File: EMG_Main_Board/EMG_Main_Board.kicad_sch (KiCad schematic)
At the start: 4 parts, among them J1 ADC input, J2 USB_C_Receptacle, U1 STM32G0B1MET6, U2 IS1871SF-102

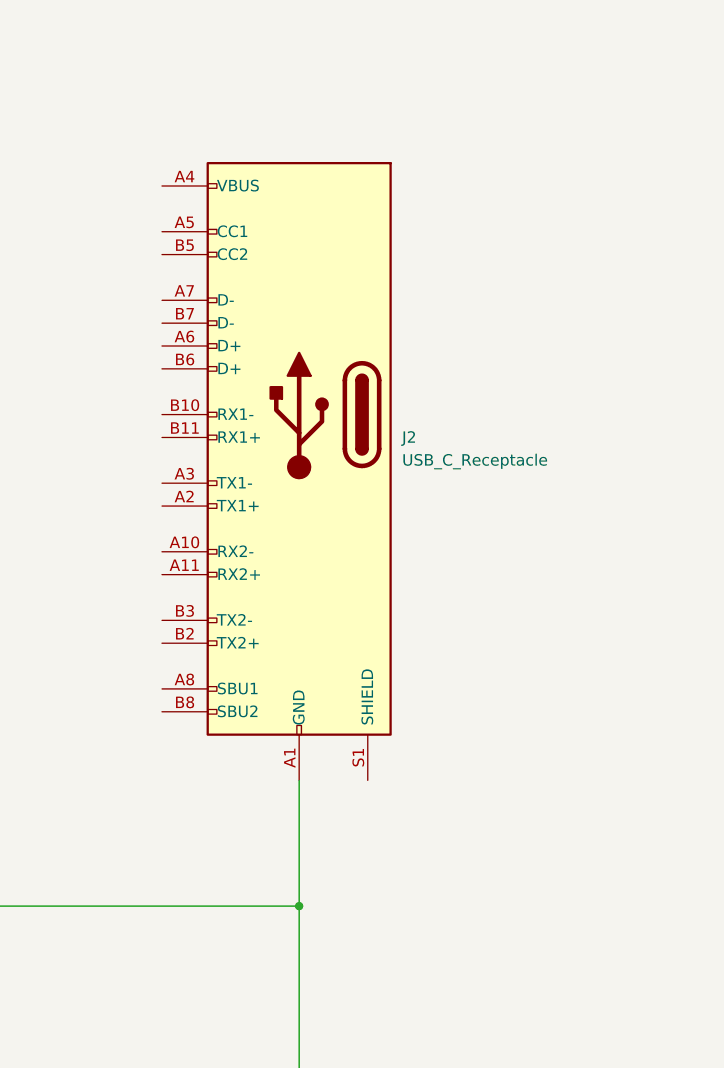
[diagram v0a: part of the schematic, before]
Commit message: add capacitor to ESD
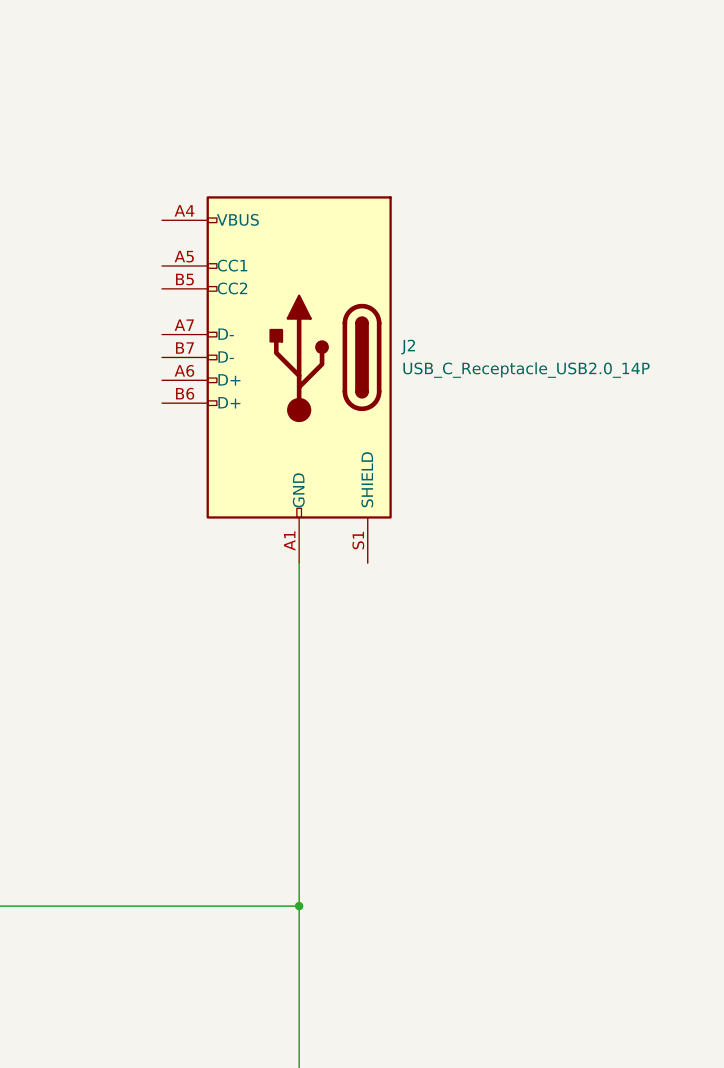
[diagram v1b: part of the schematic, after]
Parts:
- removed J2: USB_C_Receptacle, Connector_USB:USB_C_Receptacle_Amphenol_12401548E4-2A, symbol Connector:USB_C_Receptacle
- added J2: USB_C_Receptacle_USB2.0_14P, symbol Connector:USB_C_Receptacle_USB2.0_14P
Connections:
- net GND: now also J2.A1 (GND), J2.A12 (GND), J2.B1 (GND), J2.B12 (GND)
- new net: J2.A4 (VBUS), J2.A9 (VBUS), J2.B4 (VBUS), J2.B9 (VBUS)
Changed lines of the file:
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@@
 	(wire
 		(pts
-			(xy 243.84 115.57) (xy 243.84 129.54)
+			(xy 243.84 91.44) (xy 243.84 129.54)
 		)
 		(stroke
@@
 	)
 	(symbol
+		(lib_id "Connector:USB_C_Receptacle_USB2.0_14P")
+		(at 243.84 68.58 0)
+		(mirror y)
+		(unit 1)
+		(exclude_from_sim no)
+		(in_bom yes)
+		(on_board yes)
+		(dnp no)
+		(fields_autoplaced yes)
+		(property "Reference" "J2"
+			(at 255.27 67.3099 0)
+			(effects
+				(font
+					(size 1.27 1.27)
+				)
+				(justify right)
+			)
+		)
+		(property "Value" "USB_C_Receptacle_USB2.0_14P"
+			(at 255.27 69.8499 0)
+			(effects
+				(font
+					(size 1.27 1.27)
+				)
+				(justify right)
+			)
+		)
+		(property "Footprint" ""
+			(at 240.03 68.58 0)
+			(effects
+				(font
+					(size 1.27 1.27)
+				)
+				(hide yes)
+			)
+		)
+		(property "Datasheet" "https://www.usb.org/sites/default/files/documents/usb_type-c.zip"
+			(at 240.03 68.58 0)
+			(effects
+				(font
+					(size 1.27 1.27)
+				)
+				(hide yes)
+			)
+		)
+		(property "Description" "USB 2.0-only 14P Type-C Receptacle connector"
+			(at 243.84 68.58 0)
+			(effects
+				(font
+					(size 1.27 1.27)
+				)
+				(hide yes)
+			)
+		)
+		(pin "A12"
+		)
+		(pin "A4"
+		)
+		(pin "B4"
+		)
+		(pin "B6"
+		)
+		(pin "B7"
+		)
+		(pin "B5"
+		)
+		(pin "A5"
+		)
+		(pin "A1"
+		)
+		(pin "A7"
+		)
+		(pin "A9"
+		)
+		(pin "B12"
+		)
+		(pin "S1"
+		)
+		(pin "A6"
+		)
+		(pin "B1"
+		)
+		(pin "B9"
+		)
+		(instances
+			(project ""
+				(path "/f342d0b6-fa79-42c3-b491-044d5cde1fcc"
+					(reference "J2")
+					(unit 1)
+				)
+			)
+		)
+	)
+	(symbol
 		(lib_id "power:+3V3")
 		(at 113.03 24.13 0)
@@
 					(unit 1)
 				)
-			)
-		)
-	)
-	(symbol
-		(lib_id "Connector:USB_C_Receptacle")
-		(at 243.84 74.93 0)
-		(mirror y)
-		(unit 1)
-		(exclude_from_sim no)
-		(in_bom yes)
-		(on_board yes)
-		(dnp no)
-		(fields_autoplaced yes)
-		(property "Reference" "J2"
-			(at 255.27 77.4699 0)
-			(effects
-				(font
-					(size 1.27 1.27)
-				)
-				(justify right)
-			)
-		)
-		(property "Value" "USB_C_Receptacle"
-			(at 255.27 80.0099 0)
-			(effects
-				(font
-					(size 1.27 1.27)
-				)
-				(justify right)
-			)
-		)
-		(property "Footprint" "Connector_USB:USB_C_Receptacle_Amphenol_12401548E4-2A"
-			(at 240.03 74.93 0)
-			(effects
-				(font
-					(size 1.27 1.27)
-				)
-				(hide yes)
-			)
-		)
-		(property "Datasheet" "https://www.usb.org/sites/default/files/documents/usb_type-c.zip"
-			(at 240.03 74.93 0)
-			(effects
-				(font
-					(size 1.27 1.27)
-				)
-				(hide yes)
-			)
-		)
-		(property "Description" "USB Full-Featured Type-C Receptacle connector"
-			(at 243.84 74.93 0)
-			(effects
-				(font
-					(size 1.27 1.27)
-				)
-				(hide yes)
-			)
-		)
-		(pin "A1"
-		)
-		(pin "A3"
-		)
-		(pin "A6"
-		)
-		(pin "A7"
-		)
-		(pin "A9"
-		)
-		(pin "A2"
-		)
-		(pin "B12"
-		)
-		(pin "B2"
-		)
-		(pin "B3"
-		)
-		(pin "A4"
-		)
-		(pin "B4"
-		)
-		(pin "B6"
-		)
-		(pin "B11"
-		)
-		(pin "B5"
-		)
-		(pin "A5"
-		)
-		(pin "B10"
-		)
-		(pin "B1"
-		)
-		(pin "A11"
-		)
-		(pin "A8"
-		)
-		(pin "A12"
-		)
-		(pin "A10"
-		)
-		(pin "B9"
-		)
-		(pin "S1"
-		)
-		(pin "B8"
-		)
-		(pin "B7"
-		)
-		(instances
-			(project ""
-				(path "/f342d0b6-fa79-42c3-b491-044d5cde1fcc"
-					(reference "J2")
-					(unit 1)
-				)

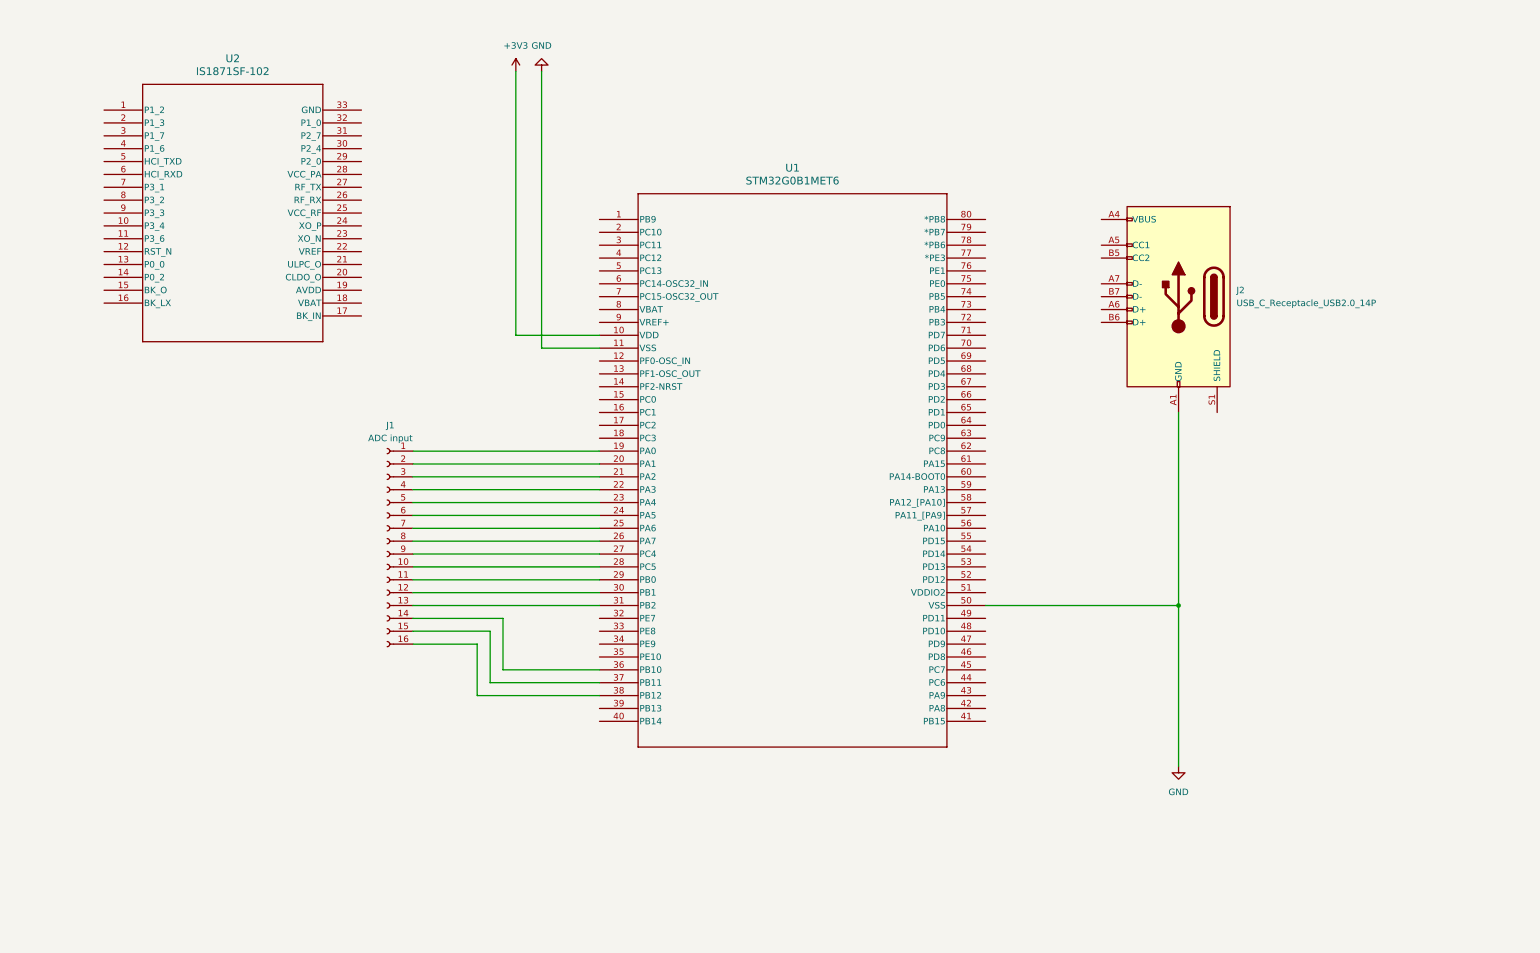
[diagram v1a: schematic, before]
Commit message: add MCU and BLE to main board schematic
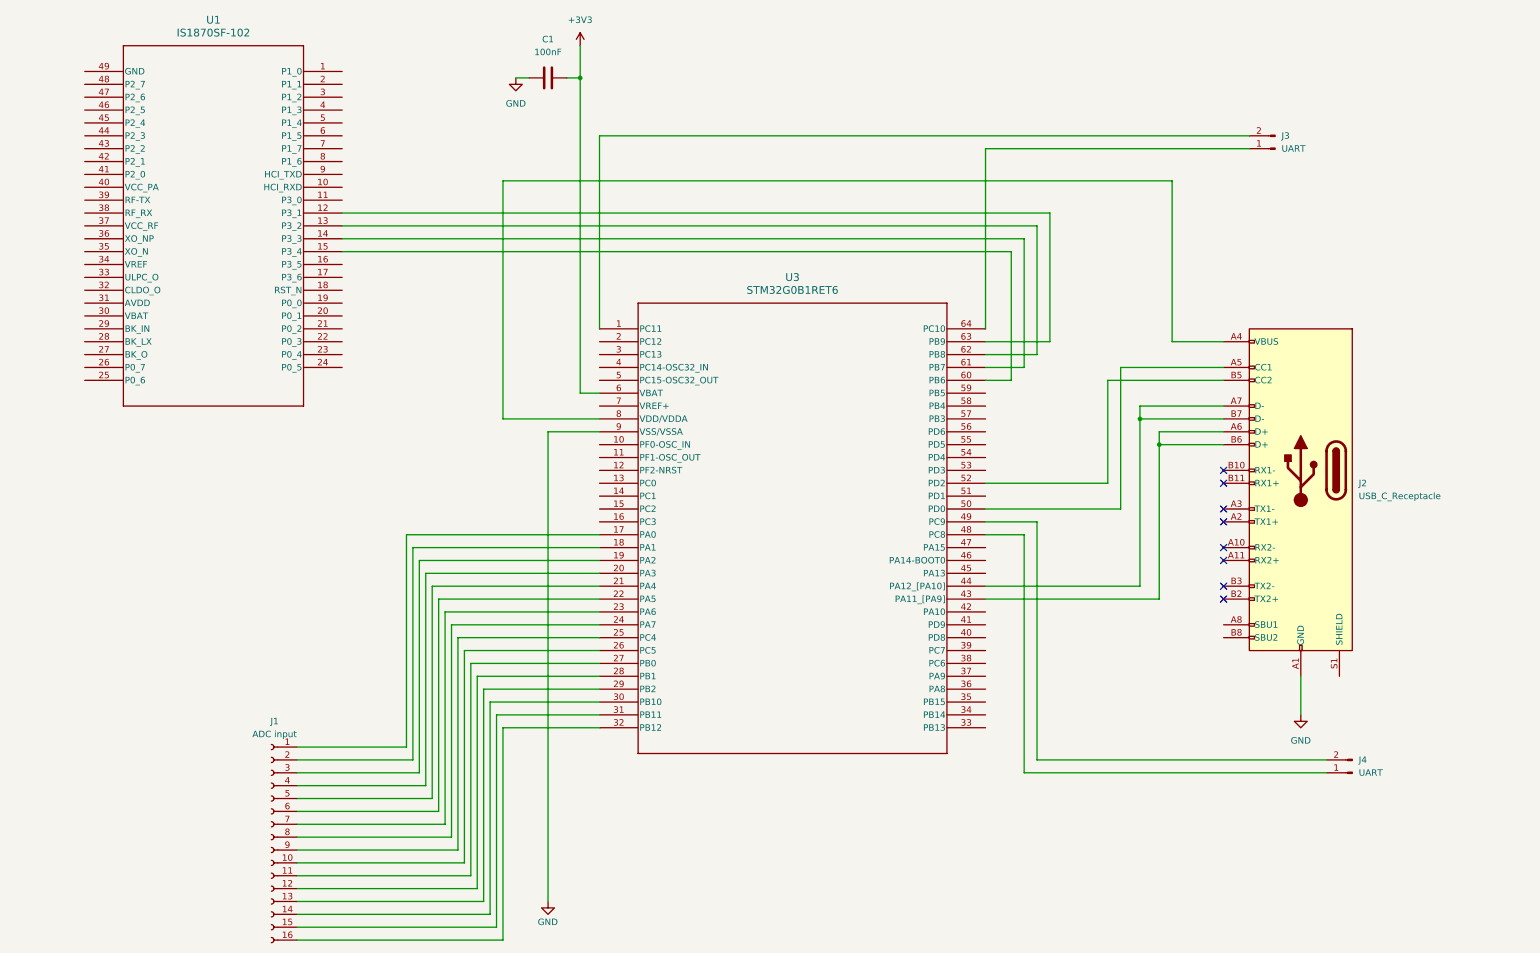
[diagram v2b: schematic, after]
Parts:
- removed J2: USB_C_Receptacle_USB2.0_14P, symbol Connector:USB_C_Receptacle_USB2.0_14P
- removed U1: STM32G0B1MET6, TQFP_0B1MET6_STM, symbol STM32G0B1MET6:STM32G0B1MET6
- removed U2: IS1871SF-102, 32QFN_4X4_IS1871SF_MCH, symbol IS1871:IS1871SF-102
- added C1: 100nF, symbol Device:C
- added J2: USB_C_Receptacle, symbol Connector:USB_C_Receptacle
- added J3, J4: UART, symbol Connector:Conn_01x02_Pin
- added U1: IS1870SF-102, 48QFN_6X6_IS1870SF_MCH, symbol IS1870SF-102:IS1870SF-102
- added U3: STM32G0B1RET6, STM32G0B1RET6:LQFP_0B1RET6_STM, symbol STM32G0B1RET6:STM32G0B1RET6
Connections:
- net +3V3: now also C1.1, U3.6 (VBAT)
- net GND: now also C1.2, J2.A1 (GND), J2.A12 (GND), J2.B1 (GND), J2.B12 (GND), U3.9 (VSS/VSSA)
- net at J1.1 (Pin_1): now also U3.17 (PA0)
- net at J1.2 (Pin_2): now also U3.18 (PA1)
- net at J1.3 (Pin_3): now also U3.19 (PA2)
- net at J1.4 (Pin_4): now also U3.20 (PA3)
- net at J1.5 (Pin_5): now also U3.21 (PA4)
- net at J1.6 (Pin_6): now also U3.22 (PA5)
- net at J1.7 (Pin_7): now also U3.23 (PA6)
- net at J1.8 (Pin_8): now also U3.24 (PA7)
- net at J1.9 (Pin_9): now also U3.25 (PC4)
- net at J1.10 (Pin_10): now also U3.26 (PC5)
- net at J1.11 (Pin_11): now also U3.27 (PB0)
- net at J1.12 (Pin_12): now also U3.28 (PB1)
- net at J1.13 (Pin_13): now also U3.29 (PB2)
- net at J1.14 (Pin_14): now also U3.30 (PB10)
- net at J1.15 (Pin_15): now also U3.31 (PB11)
- net at J1.16 (Pin_16): now also U3.32 (PB12)
- new net: J3.1 (Pin_1), U3.64 (PC10)
- new net: J3.2 (Pin_2), U3.1 (PC11)
- new net: J2.A6 (D+), J2.B6 (D+), U3.43 (PA11_[PA9])
- new net: J2.A7 (D-), J2.B7 (D-), U3.44 (PA12_[PA10])
- new net: J4.1 (Pin_1), U3.48 (PC8)
- new net: J4.2 (Pin_2), U3.49 (PC9)
- new net: J2.A5 (CC1), U3.50 (PD0)
- new net: J2.B5 (CC2), U3.52 (PD2)
- new net: U1.15 (P3_4), U3.60 (PB6)
- new net: U1.14 (P3_3), U3.61 (PB7)
- new net: U1.13 (P3_2), U3.62 (PB8)
- new net: U1.12 (P3_1), U3.63 (PB9)
- new net: J2.A4 (VBUS), J2.A9 (VBUS), J2.B4 (VBUS), J2.B9 (VBUS), U3.8 (VDD/VDDA)
- no-connect marks 0 -> 8
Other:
- moved on the sheet: J1

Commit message: add buck converter 3v3 to 1v8, start new two-board sigacq project
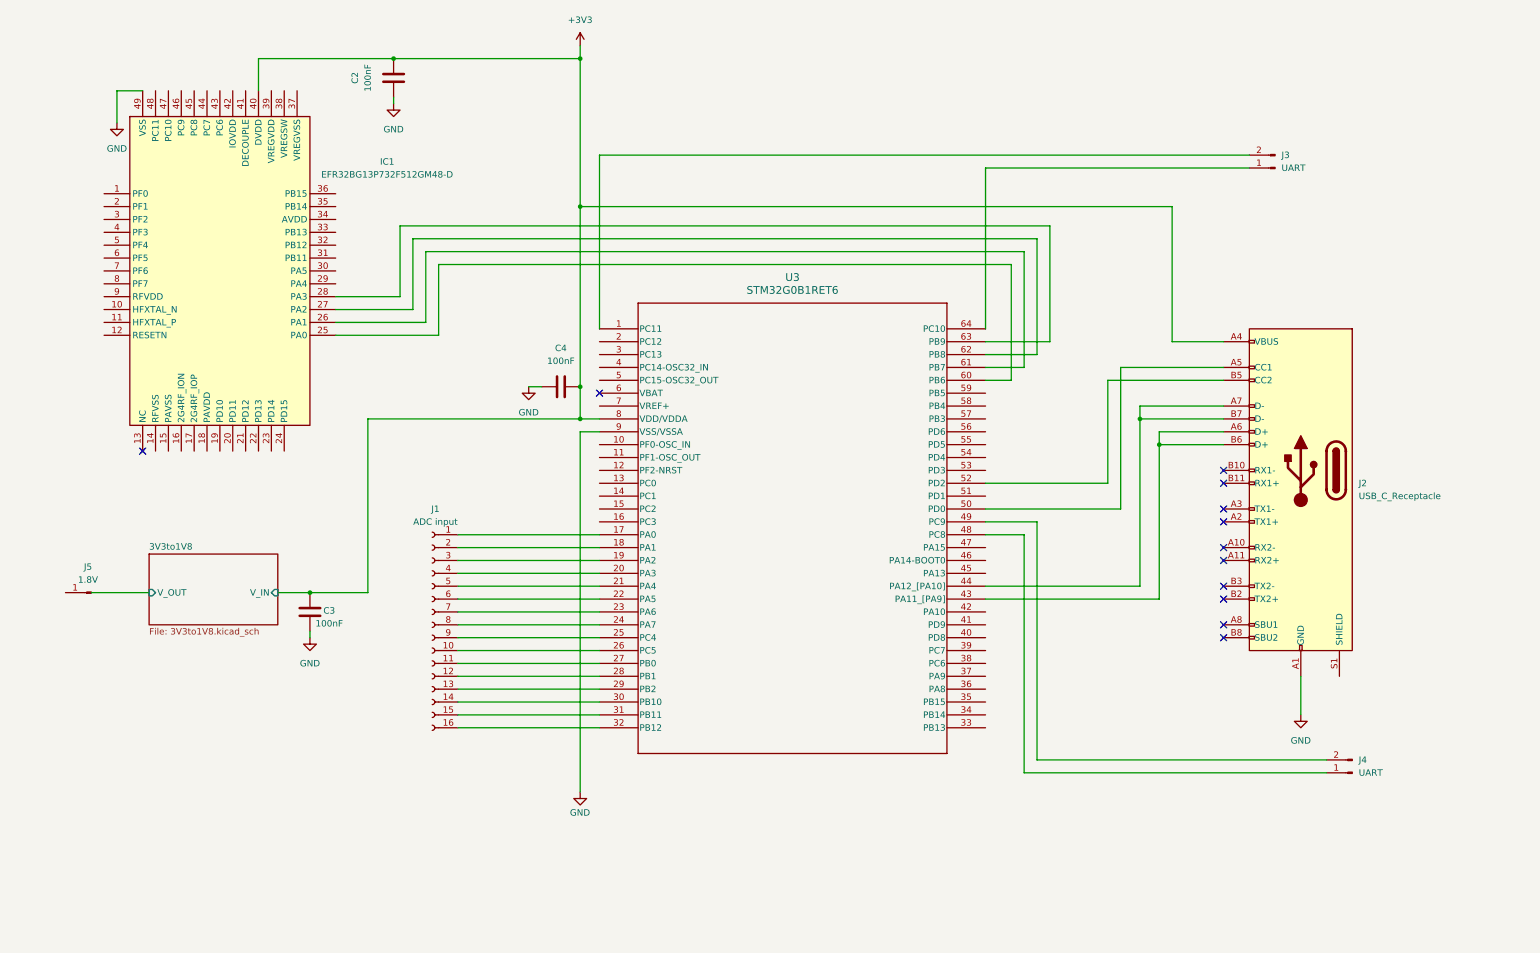
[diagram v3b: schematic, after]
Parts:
- removed C1: 100nF, symbol Device:C
- removed U1: IS1870SF-102, 48QFN_6X6_IS1870SF_MCH, symbol IS1870SF-102:IS1870SF-102
- added C2, C3, C4: 100nF, symbol Device:C
- added IC1: EFR32BG13P732F512GM48-D, EFR32BG13P732F512GM48-D:QFN50P700X700X90-49N-D, symbol EFR32BG13P732F512GM48-D:EFR32BG13P732F512GM48-D
- added J5: 1.8V, symbol Connector:Conn_01x01_Pin
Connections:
- net +3V3: now also J2.A4 (VBUS), J2.A9 (VBUS), J2.B4 (VBUS), J2.B9 (VBUS), U3.8 (VDD/VDDA), C2.1, C3.1, C4.1, IC1.40 (DVDD); no longer U3.6 (VBAT)
- net GND: now also C2.2, C3.2, C4.2, IC1.49 (VSS)
- net at U3.60 (PB6): now also IC1.25 (PA0)
- net at U3.61 (PB7): now also IC1.26 (PA1)
- net at U3.62 (PB8): now also IC1.27 (PA2)
- net at U3.63 (PB9): now also IC1.28 (PA3)
- no-connect marks 8 -> 12
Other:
- added sheet 3V3to1V8 (3V3to1V8.kicad_sch)
- moved on the sheet: J1, J3

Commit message: switch to LDO for 1v8 and add LDO for cste 3.3V pwr supply
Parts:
- added C1: 10uF, symbol Device:C
- added IC2: LD1117DT18TR, TO228P972X240-3N, symbol LD1117DT18TR:LD1117DT18TR
- added J6: Conn_01x02_Pin, symbol Connector:Conn_01x02_Pin
- added U1: LD1117S33TR_SOT223, Package_TO_SOT_SMD:SOT-223-3_TabPin2, symbol Regulator_Linear:LD1117S33TR_SOT223
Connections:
- net GND: now also C1.2, IC2.1 (GND), J6.2 (Pin_2), U1.1 (GND)
- net +3V3: no longer names the net of C2.1, C3.1, C4.1, IC1.40 (DVDD), J2.A4 (VBUS), J2.A9 (VBUS), J2.B4 (VBUS), J2.B9 (VBUS), U3.8 (VDD/VDDA)
- net +3V3: now also IC2.3 (VIN), U1.2 (VO)
- new net: J6.1 (Pin_1), U1.3 (VI)
- new net: C1.1, IC2.4 (VOUT_(TAB))
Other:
- removed sheet 3V3to1V8
- moved on the sheet: J5
